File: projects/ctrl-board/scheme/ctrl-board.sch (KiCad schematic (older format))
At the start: 122 parts, among them K1 i2c-1, K2 i2c-1, P1 PWR-IN, P2 CONN_4, P3 PWR-IN, P4 PWR-IN, P5 PWR-IN, P6 CONN_4, P7 CONN_4, P8 PWR-IN, Q1 BC847, Q10 BC847, Q11 MOS_P, Q12 MOS_P, Q13 MOS_P, Q2 BC847, Q3 BC847, Q4 BC857, Q5 MOS_P, Q6 MOS_N, Q7 BC847, Q8 BC847, Q9 BC857, U1 NCP3063, U2 L293, X1 8MHz

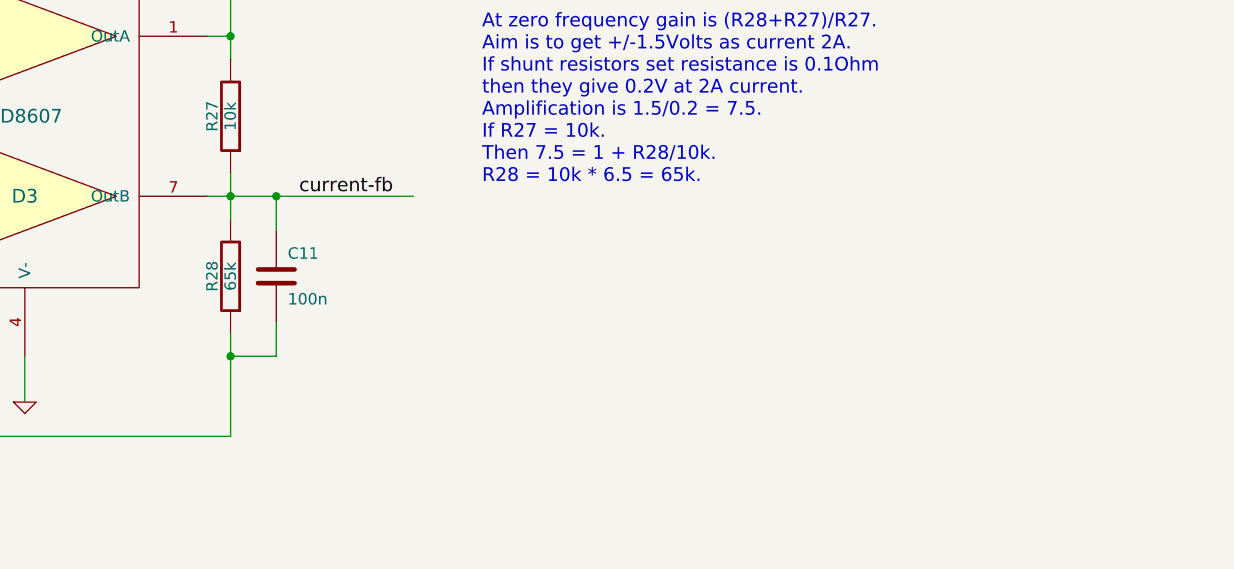
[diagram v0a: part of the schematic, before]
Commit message: Found error in current measure circuit. R27 position is not quite correct.
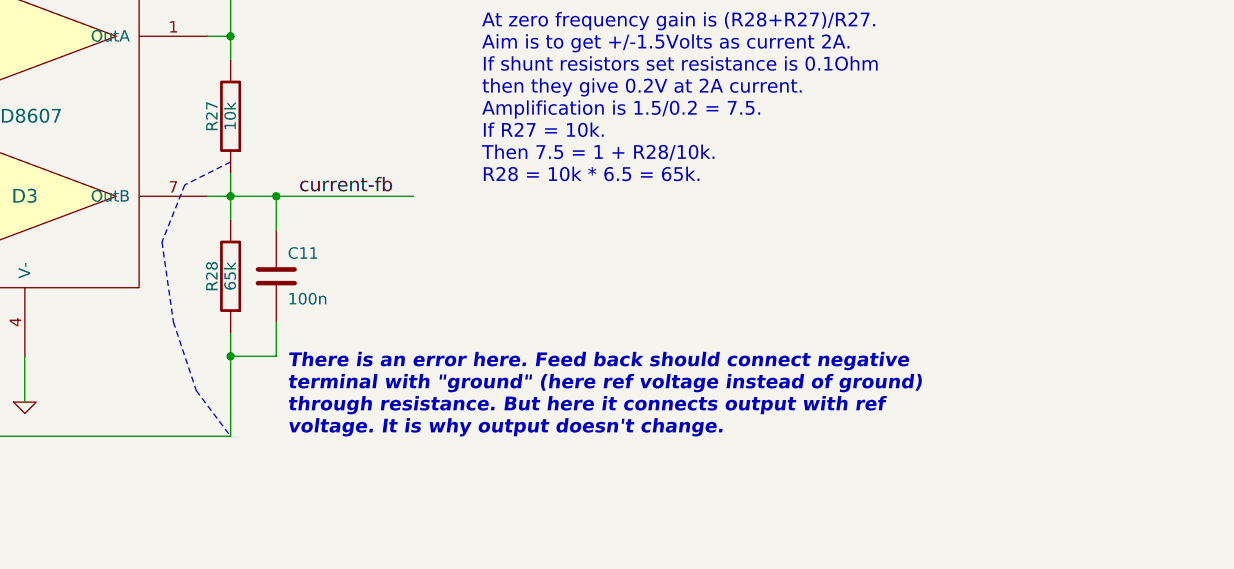
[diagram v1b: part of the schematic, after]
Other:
- note added: "There is an error here. Feed back should connect negative \nterminal with "ground" (here ref voltage instead of ground) \nthrough resistance. But here it connects output with ref \nvoltage. It is why output doesn't change."
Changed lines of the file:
@@
 Sheet 1 1
 Title ""
-Date "21 may 2013"
+Date "30 jul 2013"
 Rev ""
 Comp ""
@@
 Wire Notes Line
 	5250 18900 5950 20500
+Wire Notes Line
+	9400 20600 9200 20700
+Wire Notes Line
+	9200 20700 9100 20950
+Wire Notes Line
+	9100 20950 9150 21300
+Wire Notes Line
+	9150 21300 9250 21600
+Wire Notes Line
+	9250 21600 9400 21800
+Text Notes 9650 21800 0    60   Italic 12
+There is an error here. Feed back should connect negative \nterminal with "ground" (here ref voltage instead of ground) \nthrough resistance. But here it connects output with ref \nvoltage. It is why output doesn't change.
 $EndSCHEMATC
